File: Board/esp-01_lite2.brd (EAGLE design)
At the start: 18.4 x 51.7 mm, 17 parts, among them IC1 TINY13-20SU, K1 setup, K2 reset

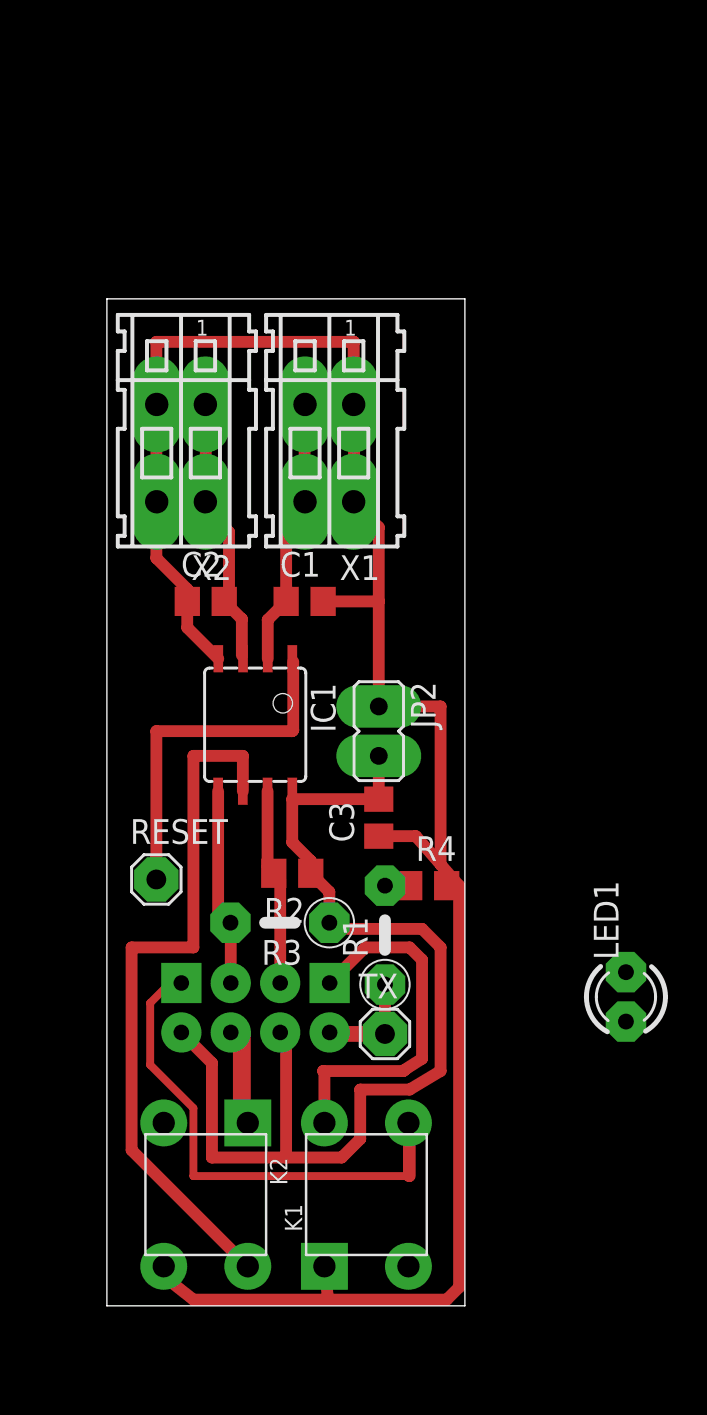
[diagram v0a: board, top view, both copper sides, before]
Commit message: add password
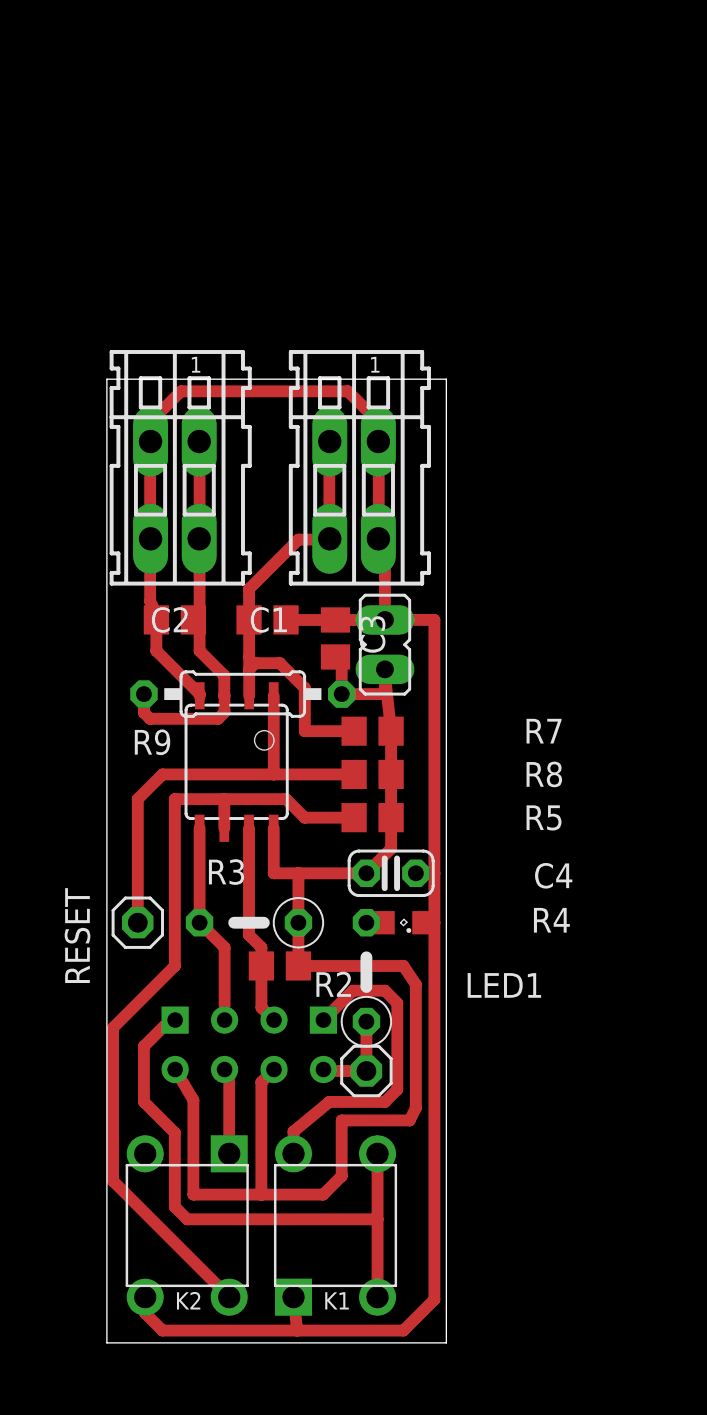
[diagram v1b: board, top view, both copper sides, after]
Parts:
- removed R1: (no value), resistor:0207/5V
- added C4: 10, resistor:C025-024X044
- added R5: 3k3, rcl:R0805
- added R7: 47k, rcl:R0805
- added R8: 10k, rcl:R0805
- added R9: 47k, resistor:0207/10
- C1, C2, C3: value (none) -> 0.1
- JP2: value (none) -> POWER
- LED1: value (none) -> RED; device led:LED3MM -> led:SML0805
- R2, R3: value (none) -> 3k3
- R4: value (none) -> 200; device rcl:R0805 -> resistor:0207/5V
- RESET: value (none) -> RESET
- TX: value (none) -> TX
- X1: value (none) -> IN1
- X2: value (none) -> IN2
- moved LED1 12.0 mm to (15.2, 21.6), turned to 180 degrees
- moved C3 9.47 mm to (11.7, 36.2), turned to 270 degrees
- moved R4 5.46 mm to (13.3, 19.1), turned to 90 degrees
- moved R2 4.80 mm to (8.89, 19.4)
- moved JP2 4.46 mm to (14.3, 35.9)
- moved RESET 2.42 mm to (1.59, 21.6)
- moved X1 2.29 mm to (12.7, 43.8)
- moved K1 2.25 mm to (11.7, 6.03)
- moved IC1 2.13 mm to (6.67, 29.8)
- moved C1 2.13 mm to (8.26, 37.1)
- moved TX 2.13 mm to (13.3, 14.0)
- moved X2 1.93 mm to (3.49, 43.8)
- moved U$1 1.93 mm to (7.30, 22.2)
- moved C2 1.85 mm to (3.49, 37.1)
- moved K2 1.85 mm to (4.13, 6.03)
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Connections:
- removed net N$1: LED1.K, R4.1
- new net N$12: LED1.A, R4.2
- net +3V3: now also C4.2, R5.1, R7.1, R8.1, R9.1
- net GND: now also C4.1, LED1.C; no longer R4.2
- net N$13: now also R8.2
- net N$15: now also R9.2
- net N$3: now also R4.1; no longer LED1.A
- net N$5: now also R5.2
- net N$9: now also R7.2
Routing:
- net +3V3: track 56.2 -> 70.6 mm
- net N$9: track 13.9 -> 24.0 mm
- net N$15: track 14.3 -> 20.3 mm
- net N$7: track 5.08 -> 0.00 mm
- net N$5: track 36.2 -> 40.5 mm
- net N$13: track 18.4 -> 22.0 mm
- net N$11: track 3.18 -> 0.00 mm
- net GND: track 105.3 -> 102.2 mm
- net N$10: track 18.8 -> 16.4 mm
- net N$12: track 0.00 -> 0.85 mm
- net N$4: track 28.3 -> 29.1 mm
- net N$8: track 5.09 -> 4.43 mm
- net N$3: track 5.41 -> 4.89 mm
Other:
- board size 18.4 x 51.7 mm -> 17.4 x 49.5 mm

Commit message: scheme
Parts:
- moved C4 3.49 mm to (11.1, 24.1)
- moved R2 3.01 mm to (7.94, 22.2)
- moved R5 2.54 mm to (11.1, 27.0)
- moved R7 2.54 mm to (11.1, 31.4)
- moved R8 2.54 mm to (11.1, 29.2)
- moved R3 1.93 mm to (7.62, 19.7)
- moved X1 1.90 mm to (10.8, 43.8)
- moved RESET 1.00 mm to (2.54, 21.9)
- moved C1 0.95 mm to (7.30, 37.1)
- moved C3 0.95 mm to (10.8, 36.2)
- moved IC1 0.95 mm to (5.71, 29.8)
- moved R4 0.95 mm to (12.4, 19.1)
- moved R9 0.95 mm to (6.03, 33.3)
- moved U$1 0.95 mm to (6.35, 22.2)
- moved C2 0.95 mm to (2.54, 37.1)
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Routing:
- net GND: track 102.2 -> 107.9 mm
- net +3V3: track 70.6 -> 67.4 mm
- net N$9: track 24.0 -> 21.4 mm
- net N$5: track 40.5 -> 42.0 mm
- net N$13: track 22.0 -> 20.8 mm
- net N$15: track 20.3 -> 21.4 mm
- net N$10: track 16.4 -> 17.5 mm
- net N$8: track 4.43 -> 5.31 mm
- net N$4: track 29.1 -> 29.6 mm
- added copper zone on layer 1, net GND

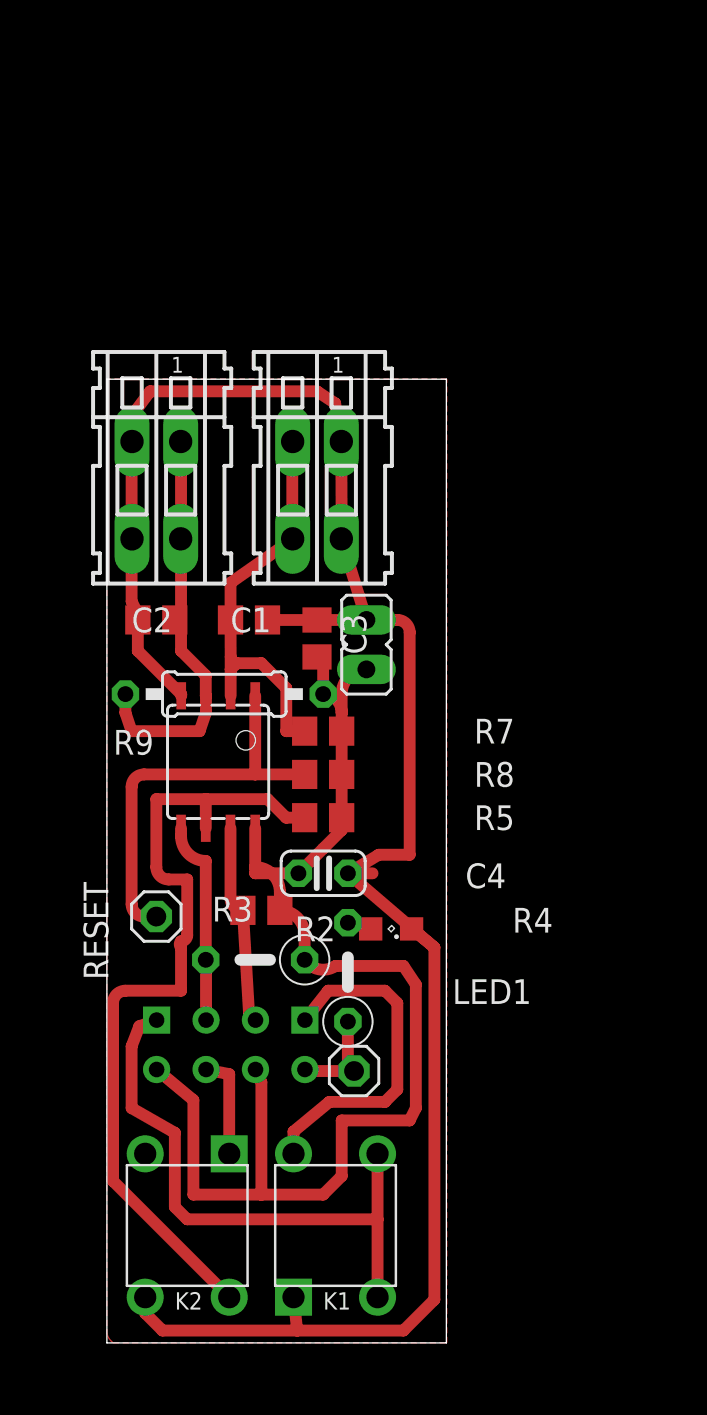
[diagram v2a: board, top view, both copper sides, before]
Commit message: attiny84 250ms check
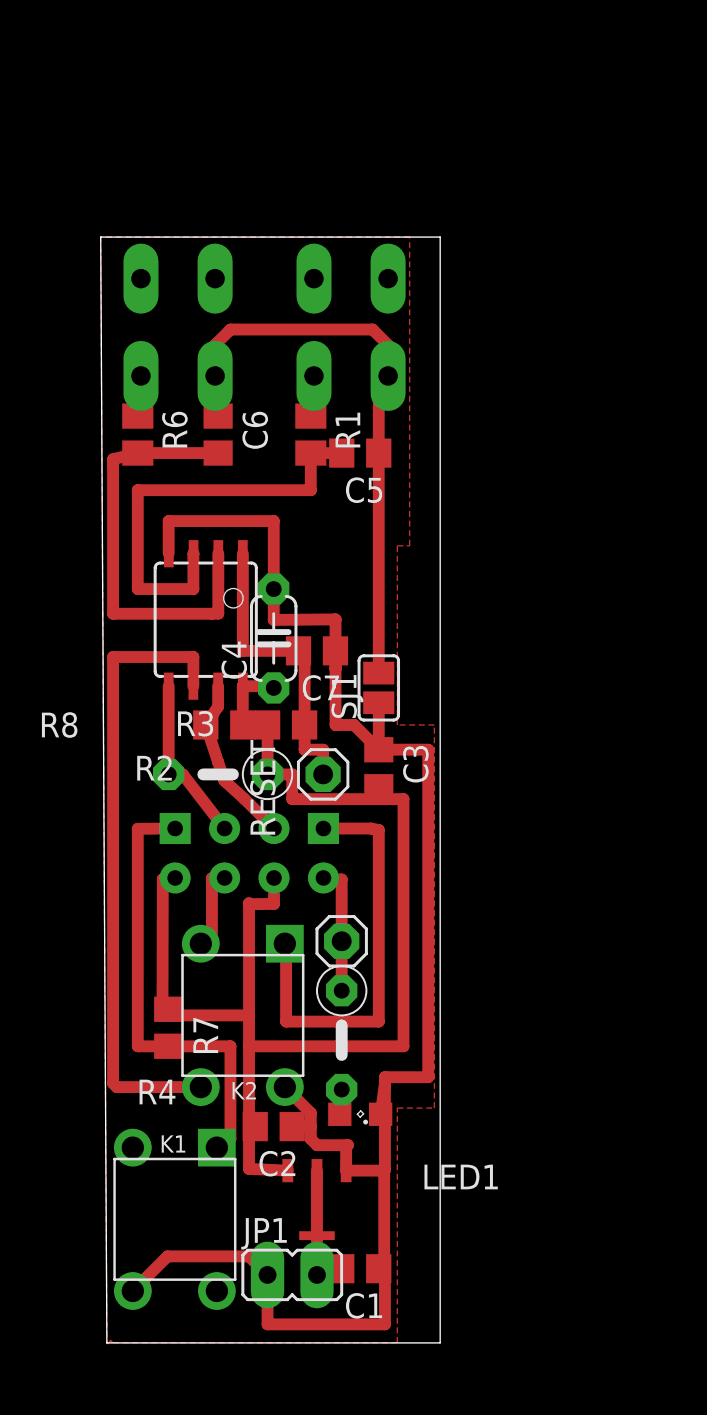
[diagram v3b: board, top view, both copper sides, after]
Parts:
- removed JP2: POWER, jumper:JP1
- removed R5: 3k3, rcl:R0805
- removed R9: 47k, resistor:0207/10
- removed TX: TX, pinhead:1X01
- added C5, C6: 0.47, resistor:C0805
- added C7: 0.1, resistor:C0805
- added JP1: (no value), jumper:JP1
- added LOG: LOG, pinhead:1X01
- added R1, R6: 3k3, resistor:M0805
- added SJ1: (no value), jumper:SJ
- added U$2: HT7333, HT7333_SOT89:SOT89
- C1, C2: value 0.1 -> 1mkF; device rcl:C0805 -> resistor:C0805
- C3: device rcl:C0805 -> resistor:C0805
- C4: value 10 -> 0.1; device resistor:C025-024X044 -> resistor:C050-024X044
- R7: value 47k -> 3k3
- X1: value IN1 -> 235-102; device con-wago:233-102 -> con-wago_235:P-235-102
- X2: value IN2 -> 235-102; device con-wago:233-102 -> con-wago_235:P-235-102
- moved C1 33.8 mm to (13.0, 3.81), turned to 180 degrees
- moved C2 26.7 mm to (8.57, 11.1), turned to 180 degrees
- moved R7 17.2 mm to (3.17, 16.2), turned to 270 degrees
- moved X2 13.7 mm to (12.7, 53.0), flipped to the bottom, turned to 90 degrees
- moved C4 12.3 mm to (8.57, 36.2), turned to 90 degrees
- moved X1 11.6 mm to (3.81, 53.0), flipped to the bottom, turned to 90 degrees
- moved RESET 11.3 mm to (11.1, 29.2)
- moved K2 11.2 mm to (6.99, 16.8)
- moved U$1 9.89 mm to (7.30, 32.1)
- moved R3 9.71 mm to (5.71, 29.2)
- moved R2 9.71 mm to (6.03, 31.8)
- moved LED1 9.66 mm to (13.0, 11.7)
- moved K1 8.26 mm to (3.49, 6.35), turned to 270 degrees
- moved C3 7.38 mm to (14.0, 29.5)
- moved IC1 7.33 mm to (5.08, 37.1)
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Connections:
- net N$2 renamed SDA
- net N$6 renamed SCK
- removed net N$10: K1.4, U$1.GND
- removed net N$15: C2.2, IC1.3, R9.2, X2.B1
- removed net N$8: K2.1, U$1.RST
- removed net N$9: C1.1, IC1.2, R7.2, X1.B2
- new net AA*3: C1.2, JP1.2, U$2.VIN
- new net GND1: K2.1, U$1.GND
- new net IN1: C6.2, IC1.2, R6.2
- new net IN2: C5.2, IC1.3, R1.2
- new net LOG: LOG.1, R4.1, U$1.TX
- new net N$2: K2.2, U$1.RST
- new net RX: K1.1, R7.2, U$1.RX
- new net WAKE_UP: IC1.6, K2.3
- net +3V3: now also C2.2, C4.1, U$2.VOUT; no longer C4.2, JP2.2, R5.1, R9.1
- net GND: now also C1.1, C4.2, C7.1, JP1.1, K1.3, K2.4, SJ1.1, U$2.GND; no longer C1.2, C4.1, JP2.1, K1.1, K2.3, X1.B1, X2.B2
- net N$13: now also C7.2
- net N$3: now also R6.1, X1.L2.2; no longer R4.1, TX.1, U$1.TX
- net N$4: now also R1.1, X2.L2.2; no longer K1.2, K1.3, U$1.RX
- net N$5: now also C5.1, C6.1, SJ1.2, X1.L1.2, X2.L1.2; no longer IC1.6, K2.4, R5.2
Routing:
- net WAKE_UP: track 0.00 -> 32.1 mm
- net N$4: track 29.6 -> 2.09 mm
- net RX: track 0.00 -> 23.5 mm
- net IN2: track 0.00 -> 22.1 mm
- net IN1: track 0.00 -> 21.9 mm
- net GND1: track 0.00 -> 21.5 mm
- net N$9: track 21.4 -> 0.00 mm
- net N$15: track 21.4 -> 0.00 mm
- net GND: track 107.9 -> 90.3 mm
- net N$10: track 17.5 -> 0.00 mm
- net N$5: track 42.0 -> 30.3 mm
- net AA*3: track 0.00 -> 6.76 mm
- net LOG: track 0.00 -> 6.66 mm
- net N$8: track 5.31 -> 0.00 mm
- net N$2: track 0.00 -> 4.65 mm
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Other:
- board size 17.4 x 49.5 mm -> 17.4 x 56.8 mm

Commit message: LED works, server ok, ESP 24h
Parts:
- moved R2 2.71 mm to (6.99, 29.2)
- moved R3 2.71 mm to (4.76, 31.8)
- moved LED1 1.71 mm to (11.4, 12.4), turned to 0 degrees
- moved C3 1.62 mm to (12.4, 29.2)
- moved R1 1.59 mm to (8.89, 46.7)
- moved RESET 1.00 mm to (10.2, 29.5), turned to 90 degrees
- moved C5 0.95 mm to (12.1, 45.7)
- moved R4 0.63 mm to (12.1, 16.2)
- moved C1 0.45 mm to (12.7, 3.49)
- moved R8 0.32 mm to (9.53, 31.8)
- moved K2 0.32 mm to (6.99, 17.1)
- turned SJ1 to 270 degrees
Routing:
- net N$5: track 30.3 -> 34.4 mm
- net GND: track 90.3 -> 93.4 mm
- net N$4: track 2.09 -> 3.66 mm
- net SDA: track 8.77 -> 10.0 mm
- net IN2: track 22.1 -> 21.2 mm
- net N$13: track 16.2 -> 15.2 mm
- net LOG: track 6.66 -> 6.03 mm
- net +3V3: track 68.0 -> 67.4 mm
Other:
- board size 17.4 x 56.8 mm -> 16.5 x 57 mm

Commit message: new board
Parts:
- added C8: 0.1, resistor:C0805
- added R5: 10k, rcl:R0805
- moved LED1 14.4 mm to (11.6, 26.7), turned to 90 degrees
- moved R7 13.0 mm to (2.92, 29.2), turned to 180 degrees
- moved RESET 10.6 mm to (10.2, 40.2)
- moved C7 10.5 mm to (10.8, 46.1)
- moved C4 10.0 mm to (8.64, 46.2)
- moved IC1 10.0 mm to (5.14, 47.1)
- moved X2 9.85 mm to (12.4, 62.9)
- moved X1 9.84 mm to (3.71, 62.9)
- moved C5 9.41 mm to (11.2, 55.1)
- moved R1 9.40 mm to (8.10, 56.0)
- moved C6 9.37 mm to (5.46, 56.0)
- moved R6 9.37 mm to (1.65, 56.0)
- moved K1 9.02 mm to (4.60, 15.3), turned to 0 degrees
- moved R2 8.73 mm to (6.73, 37.9)
- moved LOG 8.62 mm to (11.2, 29.2)
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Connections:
- removed net LOG: LOG.1, R4.1, U$1.TX
- removed net N$12: LED1.A, R4.2
- new net N$1: LED1.A, LOG.1, U$1.TX
- new net N$6: LED1.C, R4.1
- net +3V3: now also R5.1
- net GND: now also C8.1, K1.2, R4.2; no longer LED1.C
- net N$2: now also R5.2
- net RX: now also K1.4; no longer K1.1
- net WAKE_UP: now also C8.2
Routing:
- net GND: track 93.4 -> 114.9 mm
- net +3V3: track 67.4 -> 81.7 mm
- net LOG: track 6.03 -> 0.00 mm
- net N$1: track 0.00 -> 5.31 mm
- net N$2: track 4.34 -> 8.79 mm
- net WAKE_UP: track 32.1 -> 28.4 mm
- net SDA: track 10.0 -> 12.7 mm
- net N$5: track 34.4 -> 36.7 mm
- net RX: track 23.5 -> 25.7 mm
- net SCK: track 8.72 -> 10.5 mm
- net N$6: track 0.00 -> 1.69 mm
- net IN2: track 21.2 -> 19.6 mm
- net AA*3: track 6.31 -> 7.71 mm
- net N$12: track 1.35 -> 0.00 mm
- net N$4: track 3.66 -> 4.76 mm
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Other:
- board size 16.5 x 57 mm -> 16.5 x 67 mm

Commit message: board for one_button
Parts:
- removed C3, C8: 0.1, resistor:C0805
- removed K1: setup, Seeed-OPL-Button:SW4-6.0X6.0X5.0MM
- removed K2: reset, Seeed-OPL-Button:SW4-6.0X6.0X5.0MM
- removed RESET: RESET, pinhead:1X01
- removed SJ1: (no value), jumper:SJ
- removed X1, X2: 235-102, con-wago_235:P-235-102
- added C9: 10mkF, rcl:C025-030X050
- added R10: 3k3, resistor:M0805
- added R11: 200, rcl:R0805
- added RST: RST, pinhead:1X01
- added S2: (no value), switch-omron:B3F-31XX
- added X3: (no value), con-wago255:233-104
- C4: device resistor:C050-024X044 -> rcl:C0805
- R3: device resistor:0207/5V -> rcl:R0805
- R4: device resistor:0207/5V -> rcl:0207/2V
- R5: value 10k -> 3k3
- R8: value 10k -> 3k3; device rcl:R0805 -> rcl:0204/5
- U$2: value HT7333 -> MCP1700T-3302E/TT; device HT7333_SOT89:SOT89 -> MCP1700T-3302E_TT:MCP1700T-3302E/TT
- moved R3 17.0 mm to (3.33, 23.3), turned to 0 degrees
- moved LED1 16.3 mm to (10.3, 10.4), turned to 0 degrees
- moved C4 16.3 mm to (8.26, 29.9)
- moved R5 16.3 mm to (4.67, 13.2), turned to 0 degrees
- moved U$1 16.1 mm to (7.49, 23.9)
- moved LOG 16.1 mm to (11.3, 13.1)
- moved IC1 14.9 mm to (4.38, 32.2)
- moved R2 14.8 mm to (8.67, 23.3)
- moved R4 12.5 mm to (6.06, 10.5), turned to 180 degrees
- moved C7 12.0 mm to (8.22, 34.4), turned to 90 degrees
- moved C2 10.7 mm to (2.60, 8.70), turned to 0 degrees
- moved U$2 9.36 mm to (2.60, 5.40), turned to 180 degrees
- moved R7 7.98 mm to (3.33, 21.2), turned to 0 degrees
- moved C5 7.32 mm to (12.1, 47.8)
- moved R8 6.56 mm to (10.5, 30.8)
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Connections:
- removed net N$5: C5.1, C6.1, SJ1.2, X1.L1.2, X2.L1.2
- new net N$11: R5.2, U$1.RST
- net +3V3: now also C2.1; no longer C2.2, C3.2, U$1.CH_PD
- net AA*3: now also C1.1, C9.1; no longer C1.2
- net GND: now also C1.2, C2.2, C9.2, R10.2, U$1.GND; no longer C1.1, C2.1, C3.1, C8.1, K1.2, K1.3, K2.4, SJ1.1
- net GND1: now also C5.1, C6.1, R10.1, R11.2, X3.A2, X3.A4; no longer K2.1, U$1.GND
- net IN1: now also C5.2, R1.2; no longer C6.2, R6.2
- net IN2: now also C6.2, R6.2; no longer C5.2, R1.2
- net N$13: now also RST.1; no longer RESET.1
- net N$2: now also R11.1, S2.1; no longer K2.2, R5.2, U$1.RST
- net N$3: now also X3.A1; no longer X1.L2.2
- net N$4: now also X3.A3; no longer X2.L2.2
- net RX: no longer K1.4
- net SCK: now also S2.2
- net WAKE_UP: now also U$1.CH_PD; no longer C8.2, K2.3
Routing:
- net GND: track 114.9 -> 57.6 mm
- net N$5: track 36.7 -> 0.00 mm
- net GND1: track 20.7 -> 53.5 mm
- net +3V3: track 81.7 -> 51.0 mm, vias 0 -> 2
- net RX: track 25.7 -> 3.32 mm
- net SCK: track 10.5 -> 31.7 mm
- net IN2: track 19.6 -> 28.1 mm
- net N$13: track 15.6 -> 7.44 mm
- net WAKE_UP: track 28.4 -> 31.9 mm, vias 0 -> 2
- net IN1: track 22.5 -> 19.0 mm
- net N$2: track 8.79 -> 5.70 mm
- net N$11: track 0.00 -> 2.69 mm
- net AA*3: track 7.71 -> 9.99 mm
- net N$3: track 2.54 -> 3.92 mm
- net N$4: track 4.76 -> 3.79 mm
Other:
- board size 16.5 x 67 mm -> 14 x 62 mm

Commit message: update board
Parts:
- added R9: 3k3, rcl:R0805
- R10: value 3k3 -> 0
- moved R6 8.84 mm to (10.6, 50.2), turned to 0 degrees
- moved R1 8.38 mm to (2.00, 51.1), turned to 270 degrees
- moved C6 7.14 mm to (12.0, 46.6)
- moved C5 6.56 mm to (5.97, 50.2)
- moved R4 2.88 mm to (7.81, 8.19)
- moved C1 1.61 mm to (5.68, 4.16)
- moved LED1 1.60 mm to (11.3, 9.24), turned to 90 degrees
- moved C9 1.54 mm to (8.57, 3.81)
- moved JP1 1.40 mm to (11.9, 3.81)
- moved R7 0.73 mm to (3.33, 20.5)
- moved C2 0.45 mm to (2.51, 8.26)
- moved U$2 0.37 mm to (2.48, 5.05)
- moved R11 0.31 mm to (8.76, 45.6)
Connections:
- net GND: now also R9.2
- net IN1: now also C6.2, R6.2; no longer C5.2, R1.2
- net IN2: now also C5.2, R1.2; no longer C6.2, R6.2
- net N$3: now also X3.A3; no longer X3.A1
- net N$4: now also X3.A1; no longer X3.A3
- net WAKE_UP: now also R9.1
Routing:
- net GND: track 57.6 -> 61.1 mm
- net WAKE_UP: track 31.9 -> 34.8 mm
- net IN2: track 28.1 -> 26.8 mm
- net RX: track 3.32 -> 2.59 mm
- net +3V3: track 51.0 -> 51.7 mm
- net GND1: track 53.5 -> 54.1 mm
- net N$4: track 3.79 -> 3.27 mm

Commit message: board
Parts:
- R11, R4: value 200 -> 300
- R8: device rcl:0204/5 -> rcl:R0805
- moved JP1 3.58 mm to (8.32, 3.43)
- moved C9 3.10 mm to (11.7, 3.49)
- moved R8 2.47 mm to (10.1, 28.4), flipped to the bottom
- moved X3 1.82 mm to (7.65, 54.9)
- moved R6 1.59 mm to (10.1, 48.7)
- moved C5 1.56 mm to (5.43, 48.8)
- moved R1 1.41 mm to (1.56, 49.8)
- moved IC1 1.35 mm to (3.94, 31.0)
- moved C7 1.29 mm to (7.87, 33.1)
- moved RST 1.26 mm to (10.2, 34.0)
- moved C6 1.14 mm to (11.4, 45.6)
- moved C4 1.05 mm to (7.81, 28.9)
- moved U$1 1.05 mm to (7.05, 22.9)
- moved C1 1.05 mm to (5.24, 3.21)
- moved R7 1.05 mm to (2.89, 19.6)
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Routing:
- net +3V3: track 51.7 -> 41.8 mm, vias 2 -> 3
- net AA*3: track 9.92 -> 13.2 mm
- net N$13: track 7.28 -> 10.3 mm, vias 0 -> 1
- net GND: track 61.1 -> 60.2 mm
- net GND1: track 54.1 -> 53.4 mm
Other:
- board size 14 x 62 mm -> 13.5 x 60 mm
